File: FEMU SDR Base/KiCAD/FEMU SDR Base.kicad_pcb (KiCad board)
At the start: 4 copper layers, 164.8 x 186.6 mm, 63 parts, among them P10 PWM2, P11 PWM3, P12 PWM4, P13 PWM1, P14 PWM2, P15 PWM3, P16 PWM4, P17 12V, P18 GND, P19 12V, P2 SDR_Shield_1, P20 GND, P21 S0GND, P22 S1GND, P23 S0DN, P24 S1DN, P25 S0DP, P26 S1DP, P27 PWM0, P28 PWM5, P29 PWM6, P3 SDR_Shield_2, P30 PWM7, P31 PWM0, P32 PWM5, P33 PWM6, P34 PWM7, P4 12V, P5 GND, P6 12V, P7 GND, P8 Raspi_Power_Shield, P9 PWM1, U1 TPS562209, U2 SDR_1_LDO_1_2V, U3 SDR_2_LDO_1_2V, U4 SDR_1_LDO_3_3V, U5 SDR_2_LDO_3_3V

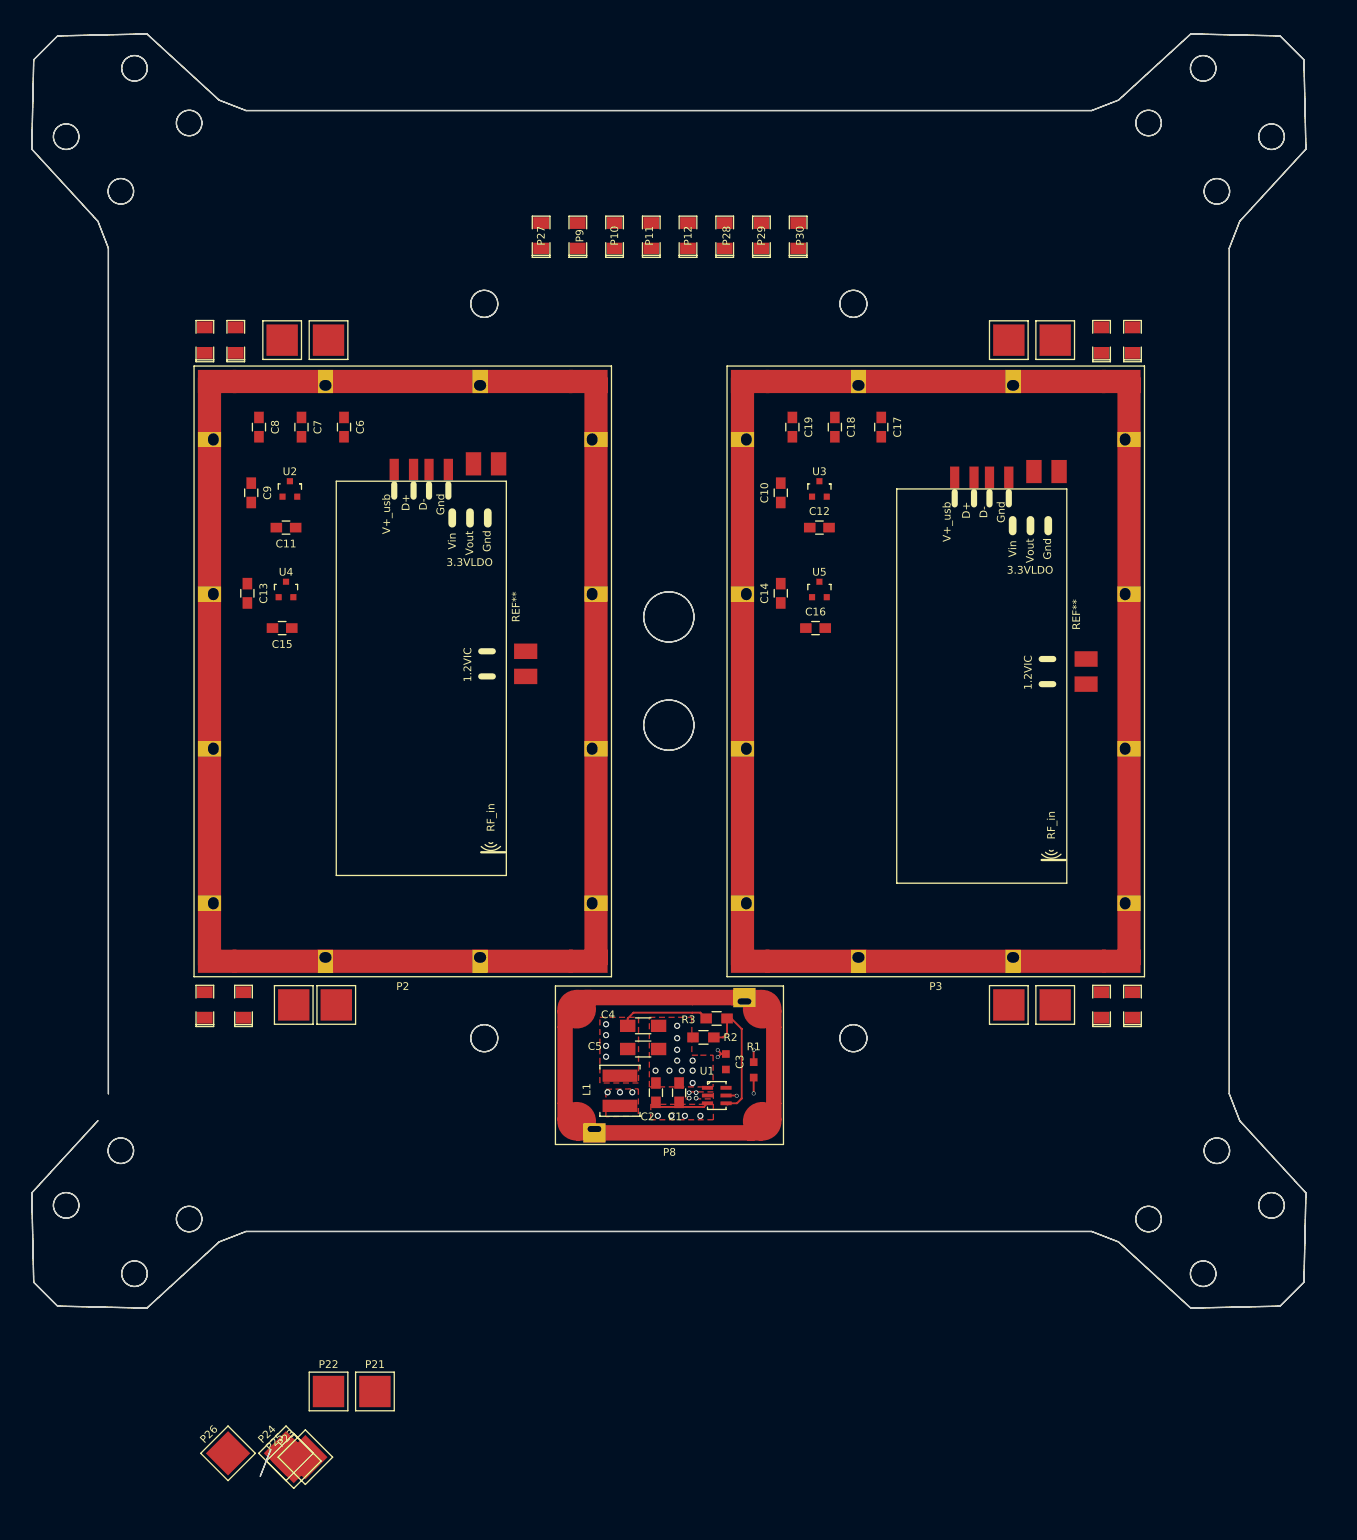
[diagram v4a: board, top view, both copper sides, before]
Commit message: Routed PWM wires and via stitched esc pads -3 hours of work...
Signed-off-by: hardiepienaar <hardiepienaar@gmail.com>
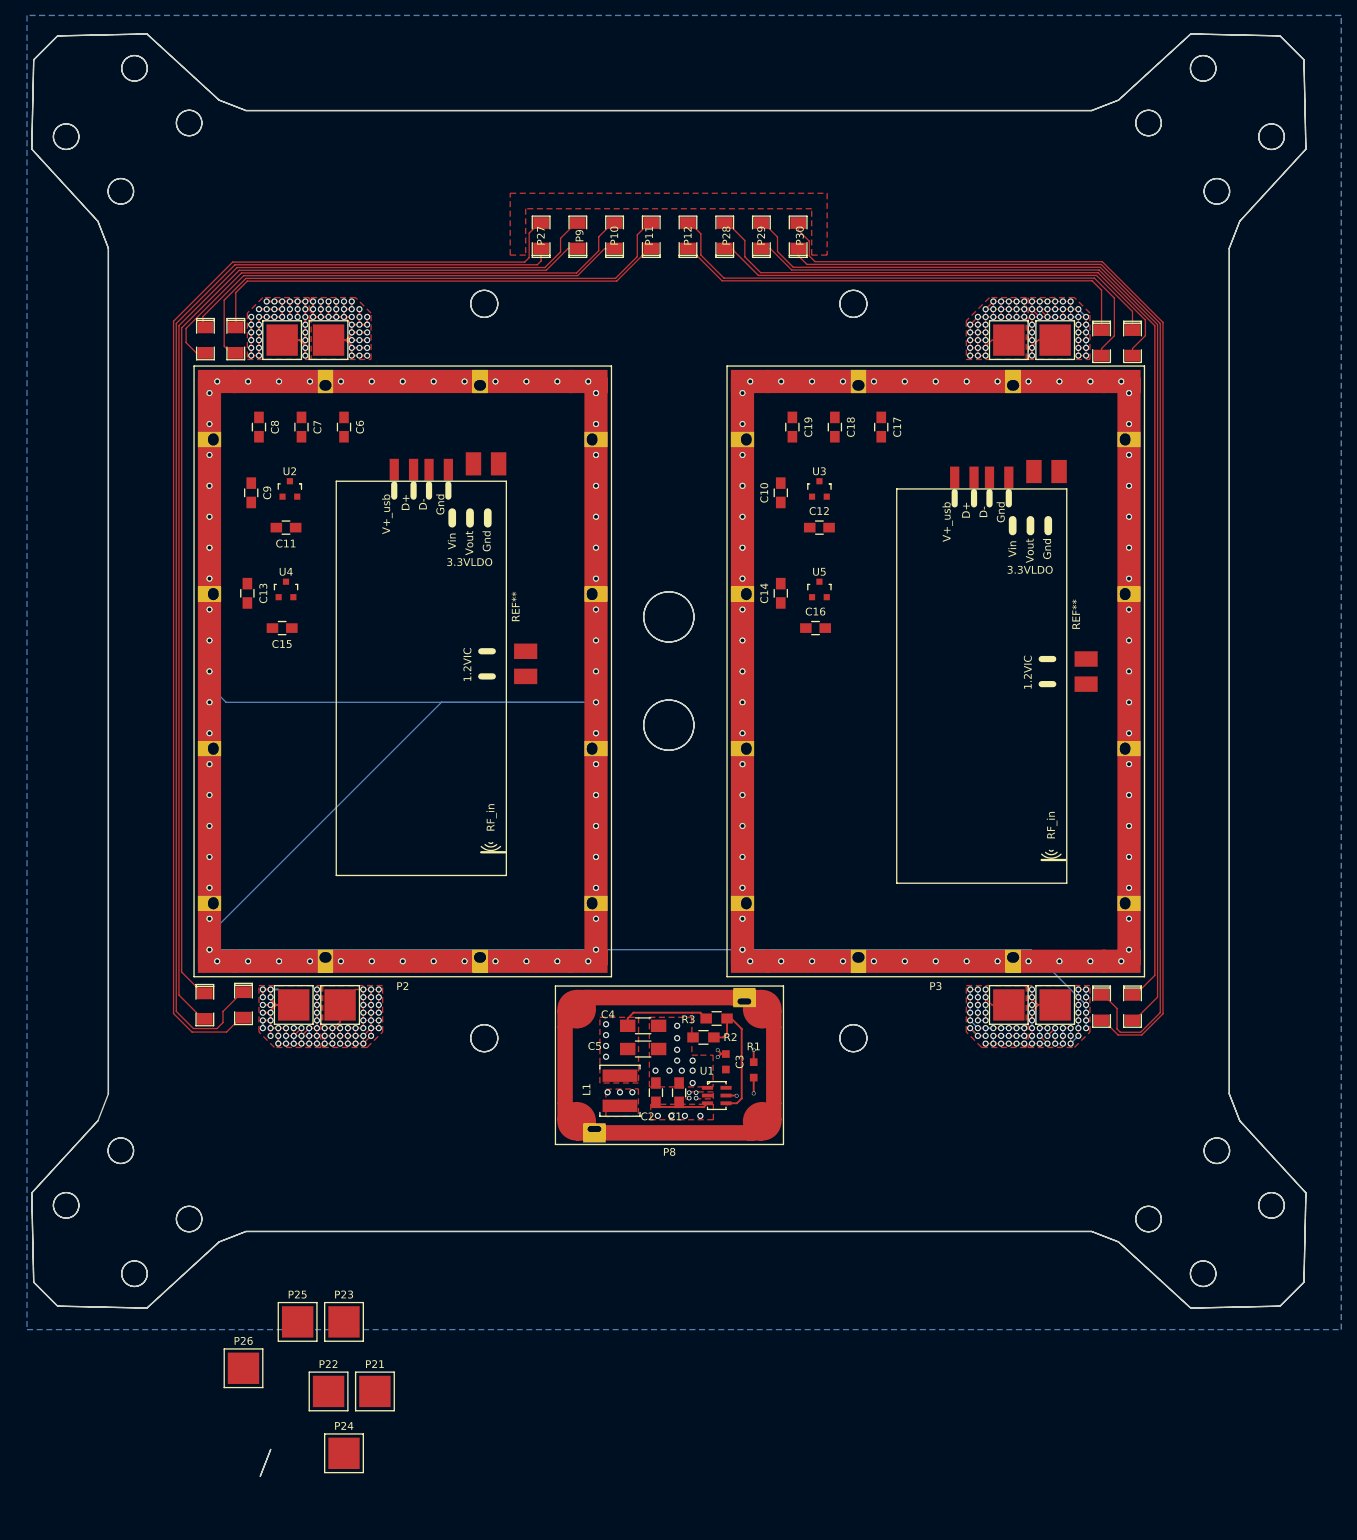
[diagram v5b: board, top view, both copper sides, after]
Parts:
- moved P23 18.2 mm to (42.5, 168.8), turned to 0 degrees
- moved P25 18.0 mm to (36.5, 168.8), turned to 0 degrees
- moved P26 11.2 mm to (29.5, 174.8), turned to 0 degrees
- moved P24 7.50 mm to (42.5, 185.8), turned to 0 degrees
- moved P13 5.00 mm to (24.5, 127.9), turned to 270 degrees
- moved P31 5.00 mm to (29.5, 127.8), turned to 270 degrees
- moved P16 4.02 mm to (140.5, 42.1), turned to 270 degrees
- moved P32 4.02 mm to (144.5, 42.1), turned to 270 degrees
- moved P6 0.50 mm to (42.0, 127.8)
- moved P33 0.35 mm to (144.5, 128.1), turned to 270 degrees
- moved P34 0.35 mm to (140.5, 128.1), turned to 270 degrees
- moved P14 0.08 mm to (24.6, 41.8), turned to 270 degrees
- turned P15 to 270 degrees
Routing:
- net GND: track 0.39 -> 896.3 mm, vias 0 -> 272
- net +12V: track 8.79 -> 210.4 mm, vias 1 -> 142
- net Net-(P27-Pad2): track 0.00 -> 154.7 mm
- net Net-(P27-Pad1): track 0.00 -> 153.6 mm
- net Net-(P30-Pad2): track 0.00 -> 153.5 mm
- net Net-(P30-Pad1): track 0.00 -> 152.8 mm
- net Net-(P29-Pad2): track 0.00 -> 149.3 mm
- net Net-(P13-Pad2): track 0.00 -> 149.1 mm
- net Net-(P13-Pad1): track 0.00 -> 143.2 mm
- net Net-(P29-Pad1): track 0.00 -> 143.0 mm
- net Net-(P11-Pad2): track 0.00 -> 69.4 mm
- net Net-(P12-Pad2): track 0.00 -> 68.9 mm
- net Net-(P10-Pad2): track 0.00 -> 66.6 mm
- net Net-(P28-Pad2): track 0.00 -> 66.1 mm
- net Net-(P12-Pad1): track 0.00 -> 60.9 mm
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- added copper zone on 12V, net +12V
- added copper zone on B.Cu, net GND
- added copper zone on F.Cu, net GND
- added copper zone on GND, net GND
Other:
- rule trace_min: 0.155 -> 0.13
- board text added: "Finish cable tray copper"
- board text added: "Finish gasket grounding Do 12V and PWR ground routing Isoate signal gnd and power ground Add power plug connections Add raspi power Add pixhawk pwr Add feedthroughs Add usb isolation Add esc wire strap mounts Add SMA grounding rings Add arm grounding rings"

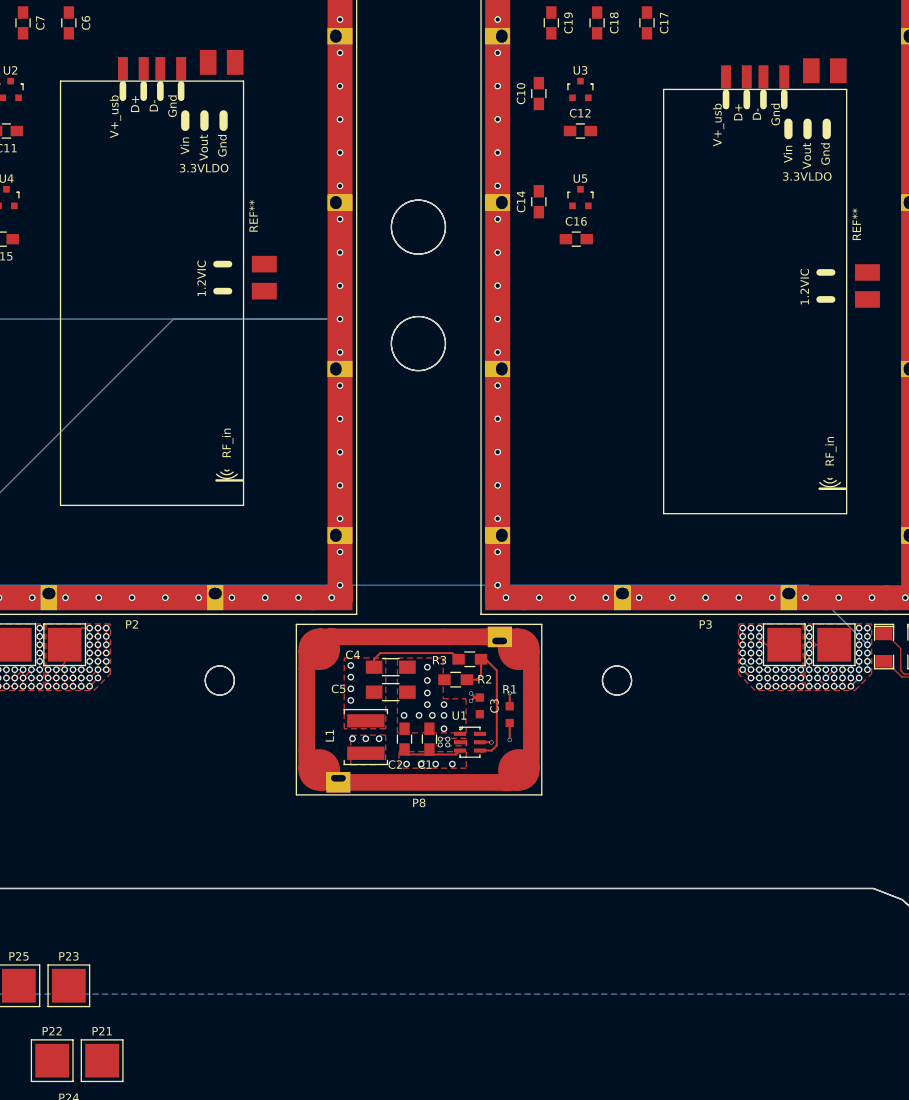
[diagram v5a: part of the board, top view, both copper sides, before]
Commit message: STATUS=FREE, Redo of RaspiPSU to avoid zone errors, trace start for +5V
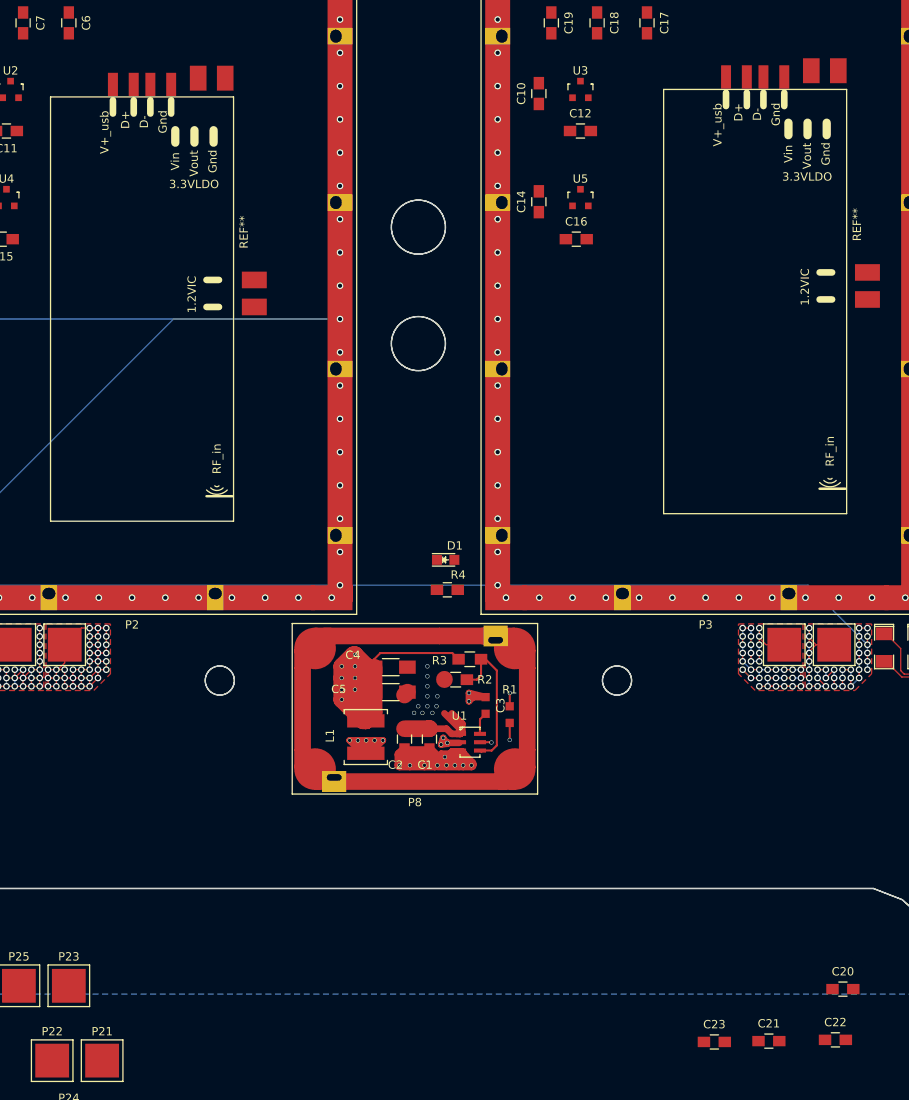
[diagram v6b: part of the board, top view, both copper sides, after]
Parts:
- added C20: 1nF, Capacitors_SMD:C_0805_HandSoldering, F.Cu at (135.6, 169.2)
- added C21: 1uF, Capacitors_SMD:C_0805_HandSoldering, F.Cu at (126.7, 175.4)
- added C22: 1uF, Capacitors_SMD:C_0805_HandSoldering, F.Cu at (134.7, 175.2)
- added C23: 10uF, Capacitors_SMD:C_0805_HandSoldering, F.Cu at (120.1, 175.5)
- added D1: LED, LEDs:LED_0805, F.Cu at (87.8, 117.5)
- added R4: 1.8k, Capacitors_SMD:C_0805_HandSoldering, F.Cu at (88.0, 121.2)
- C10, C11, C9: value 1uF -> 10uF
- C12: value 1uF -> 1nF
- U2: value SDR_1_LDO_1_2V -> LP38858-LDO
- U3: value SDR_2_LDO_1_2V -> LP38858-LDO
- U4: value SDR_1_LDO_3_3V -> 7833
- U5: value SDR_2_LDO_3_3V -> 7833
- moved REF** 2.25 mm to (40.3, 112.9)
- moved C3 0.70 mm to (92.6, 135.1)
- moved P8 0.51 mm to (84.1, 135.4)
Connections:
- C10 pad 1: GND -> +5V
- C10 pad 2: +5V -> GND
- C12 pad 1: GND -> Net-(C12-Pad1)
- C12 pad 2: +1V2_SDR2 -> GND
- U2 pad 1: GND -> Net-(C12-Pad1)
- U2 pad 2: +1V2_SDR1 -> +5V
- U2 pad 3: +5V -> GND
- U3 pad 1: GND -> Net-(C20-Pad1)
- U3 pad 2: +1V2_SDR2 -> +5V
- U3 pad 3: +5V -> GND
- U4 pad 1: GND -> (no net)
- U4 pad 2: +3V3_SDR1 -> (no net)
- U4 pad 3: +5V -> (no net)
- U5 pad 1: GND -> (no net)
- U5 pad 2: +3V3_SDR2 -> (no net)
- U5 pad 3: +5V -> (no net)
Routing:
- net +5V: track 11.7 -> 95.7 mm, vias 0 -> 8
- net /VSW: track 2.47 -> 63.6 mm, vias 2 -> 10
- net +12V: track 210.4 -> 242.4 mm, vias 142 -> 151
- net GND: track 896.3 -> 911.5 mm
- net Net-(C3-Pad2): track 0.00 -> 2.70 mm
- net (no net): track 0.00 -> 0.20 mm, vias 25 -> 11
- removed copper zone on F.Cu, net +5V
- removed copper zone on 12V, net /VSW
- removed copper zone on F.Cu, net /VSW
- removed copper zone on F.Cu, net Earth
